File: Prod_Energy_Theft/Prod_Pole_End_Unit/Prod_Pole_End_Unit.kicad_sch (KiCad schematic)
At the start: 44 parts, among them IC1 MP1584EN-LF-Z, J6 Jack-DC, J7 SS-52400-002, U1 TPS7A2033PDBVR, U10 TPS54331DG4, U3 BD00FC0WEFJ

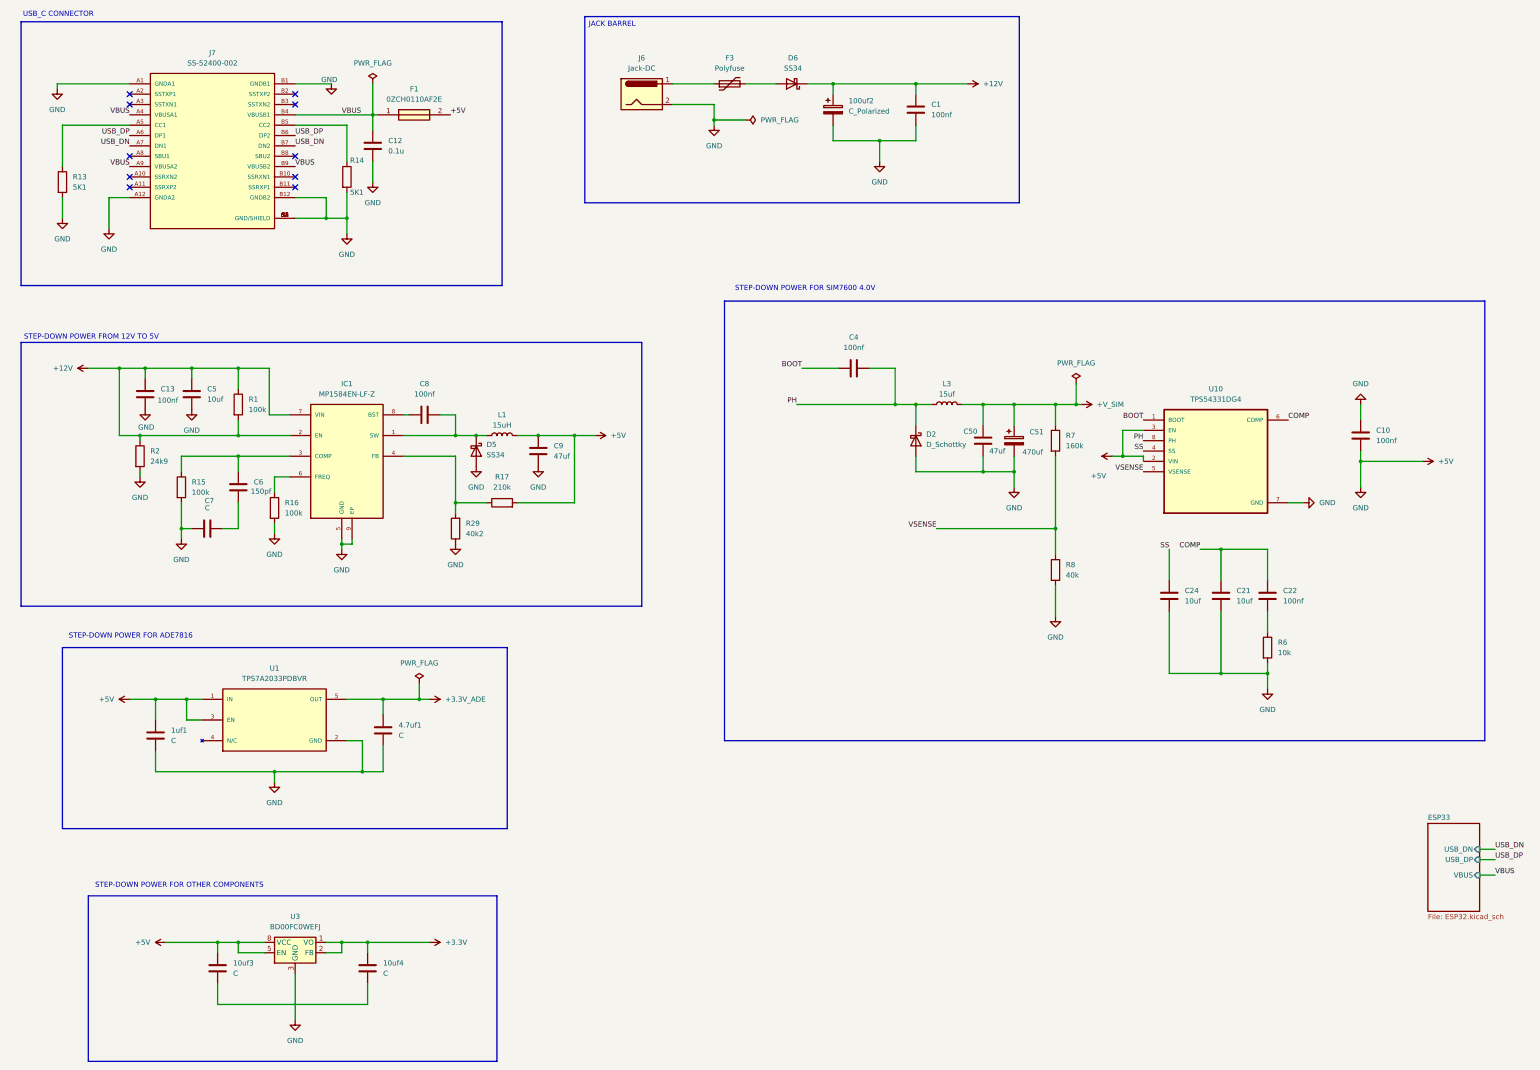
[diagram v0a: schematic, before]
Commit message: Chnages in power and ADE7816
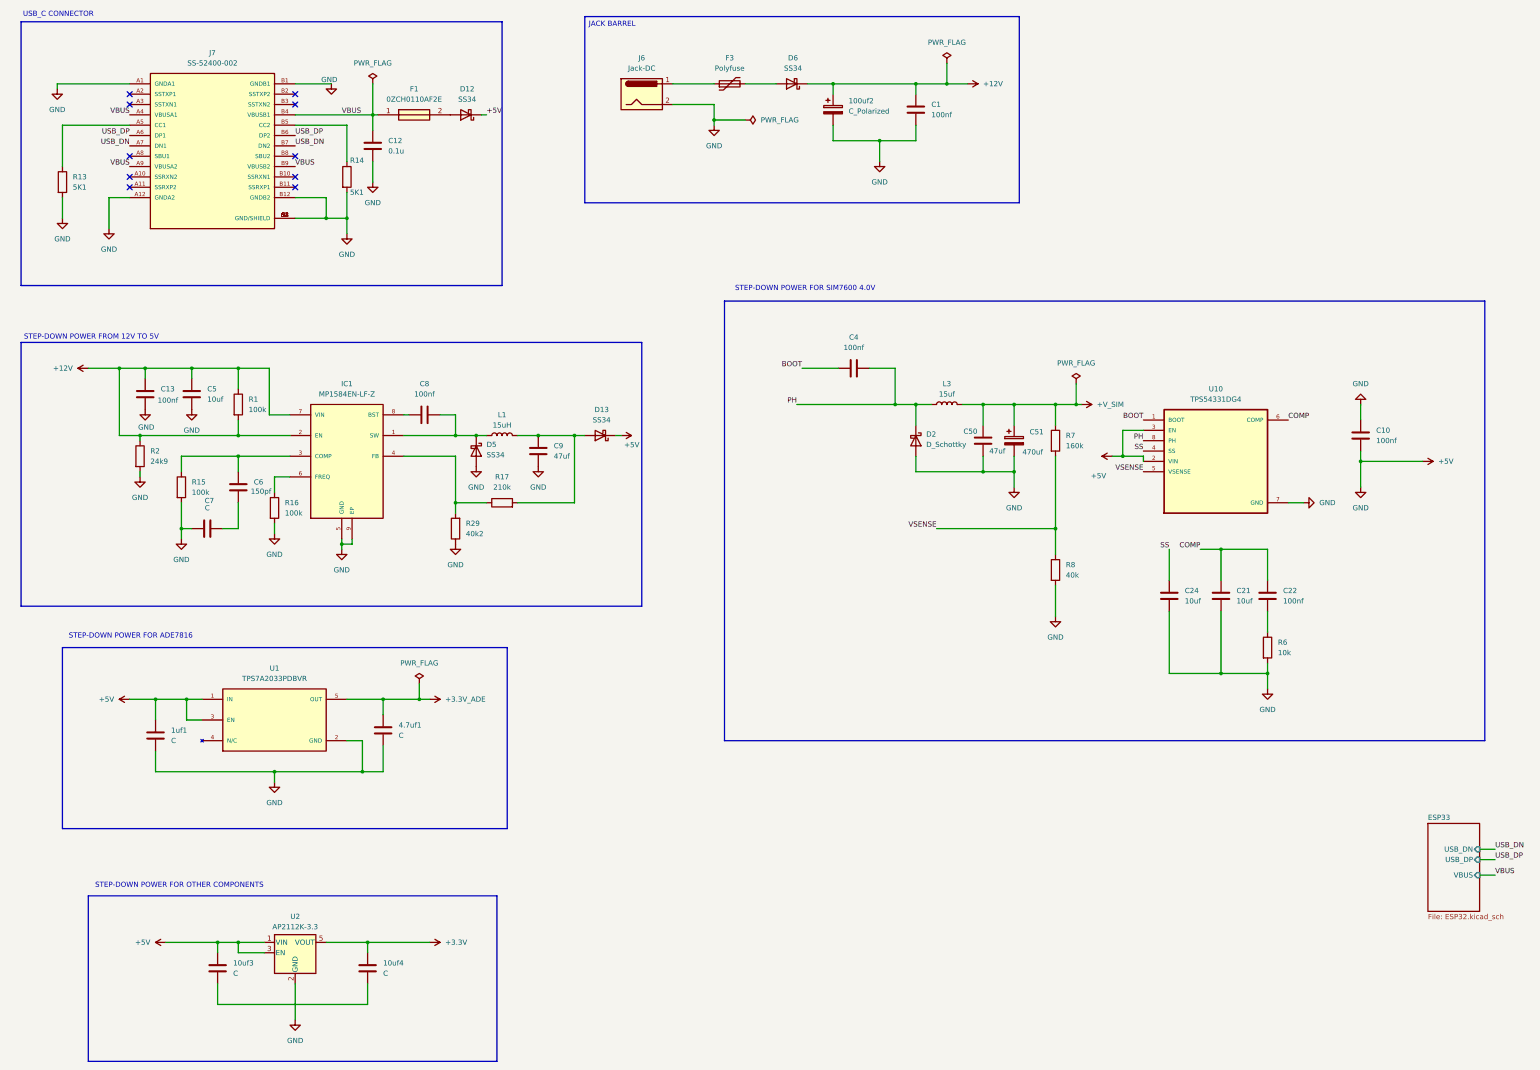
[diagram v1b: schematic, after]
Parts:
- removed U3: BD00FC0WEFJ, Package_SO:HTSOP-8-1EP_3.9x4.9mm_P1.27mm_EP2.4x3.2mm, symbol Regulator_Linear:BD00FC0WEFJ
- added D12, D13: SS34, Diode_SMD:D_SMA, symbol Diode:SS34
- added U2: AP2112K-3.3, Package_TO_SOT_SMD:SOT-23-5, symbol Regulator_Linear:AP2112K-3.3
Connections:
- net +3.3V: now also U2.5 (VOUT)
- net +5V: now also D12.1 (K), D13.1 (K), U2.1 (VIN), U2.2 (GND), U2.3 (EN); no longer C9.1, F1.2, L1.2, R17.2
- new net: D12.2 (A), F1.2
- new net: C9.1, D13.2 (A), L1.2, R17.2

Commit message: PCB
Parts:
- D2: footprint (none) -> Diode_SMD:D_SMA
- F1: footprint Footprints.kicad_mod:FUSC3226X100N -> theftdetection:FUSC3226X100N
- IC1: footprint MP1584EN-LF-Z:SOIC127P600X170-9N -> theftdetection:SOIC127P600X170-9N
- J7: footprint SS-52400-002:BELFUSE_SS-52400-002 -> theftdetection:BELFUSE_SS-52400-002
- U1: footprint TPS7A2033PDBVR:SOT95P280X145-5N -> theftdetection:SOT95P280X145-5N
- U10: footprint TPS54331DG4:SOIC127P599X175-8N -> theftdetection:SOIC127P599X175-8N
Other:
- moved on the sheet: 100uf2, C1, D6, F3, J6

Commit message: PCB Design
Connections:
- net +5V: no longer 100uf2.2, 1uf1.2, 4.7uf1.2, C1.2, C10.2, C12.2, C13.2, C21.2, C24.2, C5.2, C50.2, C51.2, C7.1, C9.2, D2.2 (A), D5.2 (A), IC1.5 (GND), IC1.9 (EP), J6.2, J7.A1 (GNDA1), J7.A12 (GNDA2), J7.B1 (GNDB1), J7.B12 (GNDB2), J7.G1 (GND/SHIELD), J7.G2 (GND/SHIELD), J7.G3 (GND/SHIELD), J7.G4 (GND/SHIELD), J7.S1 (GND/SHIELD), J7.S2 (GND/SHIELD), J7.S3 (GND/SHIELD), J7.S4 (GND/SHIELD), R13.2, R14.2, R15.2, R16.2, R2.2, R29.1, R6.2, R8.2, U1.2 (GND), U10.7 (GND), U2.2 (GND)
- new net GND: 100uf2.2, 1uf1.2, 4.7uf1.2, C1.2, C10.2, C12.2, C13.2, C21.2, C24.2, C5.2, C50.2, C51.2, C7.1, C9.2, D2.2 (A), D5.2 (A), IC1.5 (GND), IC1.9 (EP), J6.2, J7.A1 (GNDA1), J7.A12 (GNDA2), J7.B1 (GNDB1), J7.B12 (GNDB2), J7.G1 (GND/SHIELD), J7.G2 (GND/SHIELD), J7.G3 (GND/SHIELD), J7.G4 (GND/SHIELD), J7.S1 (GND/SHIELD), J7.S2 (GND/SHIELD), J7.S3 (GND/SHIELD), J7.S4 (GND/SHIELD), R13.2, R14.2, R15.2, R16.2, R2.2, R29.1, R6.2, R8.2, U1.2 (GND), U10.7 (GND), U2.2 (GND)
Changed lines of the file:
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@@
 	)
 	(junction
+		(at 349.25 116.84)
+		(diameter 0)
+		(color 0 0 0 0)
+	)
+	(junction
 		(at 73.66 129.54)
 		(diameter 0)
@@
 	)
 	(junction
-		(at 349.25 130.81)
-		(diameter 0)
-		(color 0 0 0 0)
-	)
-	(junction
 		(at 73.66 248.92)
 		(diameter 0)
@@
 	(wire
 		(pts
+			(xy 349.25 116.84) (xy 349.25 120.65)
+		)
+		(stroke
+			(width 0)
+			(type default)
+		)
+	)
+	(wire
+		(pts
 			(xy 248.92 41.91) (xy 257.81 41.91)
 		)
@@
 	(wire
 		(pts
-			(xy 349.25 130.81) (xy 364.49 130.81)
-		)
-		(stroke
-			(width 0)
-			(type default)
-		)
-	)
-	(wire
-		(pts
 			(xy 104.14 199.39) (xy 104.14 207.01)
 		)
@@
 	(wire
 		(pts
+			(xy 349.25 114.3) (xy 349.25 116.84)
+		)
+		(stroke
+			(width 0)
+			(type default)
+		)
+	)
+	(wire
+		(pts
 			(xy 55.88 248.92) (xy 68.58 248.92)
 		)
@@
 	(wire
 		(pts
-			(xy 349.25 116.84) (xy 349.25 120.65)
-		)
-		(stroke
-			(width 0)
-			(type default)
-		)
-	)
-	(wire
-		(pts
 			(xy 234.95 116.84) (xy 240.03 116.84)
 		)
@@
 	(wire
 		(pts
-			(xy 210.82 116.84) (xy 234.95 116.84)
+			(xy 349.25 116.84) (xy 354.33 116.84)
 		)
 		(stroke
@@
 	(wire
 		(pts
-			(xy 349.25 130.81) (xy 349.25 137.16)
+			(xy 210.82 116.84) (xy 234.95 116.84)
 		)
 		(stroke
@@
 	(wire
 		(pts
-			(xy 349.25 128.27) (xy 349.25 130.81)
+			(xy 349.25 128.27) (xy 349.25 137.16)
 		)
 		(stroke
@@
 	)
 	(symbol
+		(lib_id "power:+5V")
+		(at 349.25 114.3 0)
+		(unit 1)
+		(exclude_from_sim no)
+		(in_bom yes)
+		(on_board yes)
+		(dnp no)
+		(fields_autoplaced yes)
+		(property "Reference" "#PWR02"
+			(at 349.25 118.11 0)
+			(effects
+				(font
+					(size 1.27 1.27)
+				)
+				(hide yes)
+			)
+		)
+		(property "Value" "+5V"
+			(at 349.25 109.22 0)
+			(effects
+				(font
+					(size 1.27 1.27)
+				)
+			)
+		)
+		(property "Footprint" ""
+			(at 349.25 114.3 0)
+			(effects
+				(font
+					(size 1.27 1.27)
+				)
+				(hide yes)
+			)
+		)
+		(property "Datasheet" ""
+			(at 349.25 114.3 0)
+			(effects
+				(font
+					(size 1.27 1.27)
+				)
+				(hide yes)
+			)
+		)
+		(property "Description" "Power symbol creates a global label with name \"+5V\""
+			(at 349.25 114.3 0)
+			(effects
+				(font
+					(size 1.27 1.27)
+				)
+				(hide yes)
+			)
+		)
+		(pin "1"
+		)
+		(instances
+			(project ""
+				(path "/6f618807-d67d-4ead-90e4-cf8a7a59b747"
+					(reference "#PWR02")
+					(unit 1)
+				)
+			)
+		)
+	)
+	(symbol
 		(lib_id "power:GND")
 		(at 49.53 134.62 0)
@@
 	(symbol
 		(lib_id "power:GND")
-		(at 349.25 116.84 180)
-		(unit 1)
-		(exclude_from_sim no)
-		(in_bom yes)
-		(on_board yes)
-		(dnp no)
-		(fields_autoplaced yes)
-		(property "Reference" "#PWR020"
-			(at 349.25 110.49 0)
-			(effects
-				(font
-					(size 1.27 1.27)
-				)
-				(hide yes)
-			)
-		)
-		(property "Value" "GND"
-			(at 349.25 111.76 0)
-			(effects
-				(font
-					(size 1.27 1.27)
-				)
-			)
-		)
-		(property "Footprint" ""
-			(at 349.25 116.84 0)
-			(effects
-				(font
-					(size 1.27 1.27)
-				)
-				(hide yes)
-			)
-		)
-		(property "Datasheet" ""
-			(at 349.25 116.84 0)
-			(effects
-				(font
-					(size 1.27 1.27)
-				)
-				(hide yes)
-			)
-		)
-		(property "Description" "Power symbol creates a global label with name \"GND\" , ground"
-			(at 349.25 116.84 0)
-			(effects
-				(font
-					(size 1.27 1.27)
-				)
-				(hide yes)
-			)
-		)
-		(pin "1"
-		)
-		(instances
-			(project "Prod_Pole_End_Unit"
-				(path "/6f618807-d67d-4ead-90e4-cf8a7a59b747"
-					(reference "#PWR020")
-					(unit 1)
-				)
-			)
-		)
-	)
-	(symbol
-		(lib_id "power:GND")
 		(at 96.52 38.1 0)
 		(unit 1)
@@
 	)
 	(symbol
-		(lib_id "power:+12C")
-		(at 364.49 130.81 270)
-		(unit 1)
-		(exclude_from_sim no)
-		(in_bom yes)
-		(on_board yes)
-		(dnp no)
-		(fields_autoplaced yes)
-		(property "Reference" "#PWR081"
-			(at 360.68 130.81 0)
-			(effects
-				(font
-					(size 1.27 1.27)
-				)
-				(hide yes)
-			)
-		)
-		(property "Value" "+5V"
-			(at 368.3 130.8099 90)
-			(effects
-				(font
-					(size 1.27 1.27)
-				)
-				(justify left)
-			)
-		)
-		(property "Footprint" ""
-			(at 364.49 130.81 0)
-			(effects
-				(font
-					(size 1.27 1.27)
-				)
-				(hide yes)
-			)
-		)
-		(property "Datasheet" ""
-			(at 364.49 130.81 0)
-			(effects
-				(font
-					(size 1.27 1.27)
-				)
-				(hide yes)
-			)
-		)
-		(property "Description" "Power symbol creates a global label with name \"+12C\""
-			(at 364.49 130.81 0)
-			(effects
-				(font
-					(size 1.27 1.27)
-				)
-				(hide yes)
-			)
-		)
-		(pin "1"
-		)
-		(instances
-			(project "Prod_Pole_End_Unit"
-				(path "/6f618807-d67d-4ead-90e4-cf8a7a59b747"
-					(reference "#PWR081")
-					(unit 1)
-				)
-			)
-		)
-	)
-	(symbol
 		(lib_id "power:GND")
 		(at 240.03 60.96 0)
@@
 					(unit 1)
 				)
+			)
+		)
+	)
+	(symbol
+		(lib_id "power:PWR_FLAG")
+		(at 354.33 116.84 270)
+		(unit 1)
+		(exclude_from_sim no)
+		(in_bom yes)
+		(on_board yes)
+		(dnp no)
+		(fields_autoplaced yes)
+		(property "Reference" "#FLG011"
+			(at 356.235 116.84 0)
+			(effects
+				(font
+					(size 1.27 1.27)
+				)
+				(hide yes)
+			)
+		)
+		(property "Value" "PWR_FLAG"
+			(at 358.14 116.8399 90)
+			(effects
+				(font
+					(size 1.27 1.27)
+				)
+				(justify left)
+			)
+		)
+		(property "Footprint" ""
+			(at 354.33 116.84 0)
+			(effects
+				(font
+					(size 1.27 1.27)
+				)
+				(hide yes)
+			)
+		)
+		(property "Datasheet" "~"
+			(at 354.33 116.84 0)
+			(effects
+				(font
+					(size 1.27 1.27)
+				)
+				(hide yes)
+			)
+		)
+		(property "Description" "Special symbol for telling ERC where power comes from"
+			(at 354.33 116.84 0)
+			(effects
+				(font
+					(size 1.27 1.27)
+				)
+				(hide yes)
+			)
+		)
+		(pin "1"
+		)
+		(instances
+			(project "Prod_Pole_End_Unit"
+				(path "/6f618807-d67d-4ead-90e4-cf8a7a59b747"
+					(reference "#FLG011")
+					(unit 1)
+				)
